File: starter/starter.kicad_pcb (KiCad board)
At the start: 2 copper layers, 70.6 x 59.9 mm, 35 parts, among them J1 Conn_01x04_MountingPin, J2 Conn_01x02, Q1 Q_NMOS_GDS, U1 MCP1416, U2 LM1117DT-ADJ, U3 TLC555xD

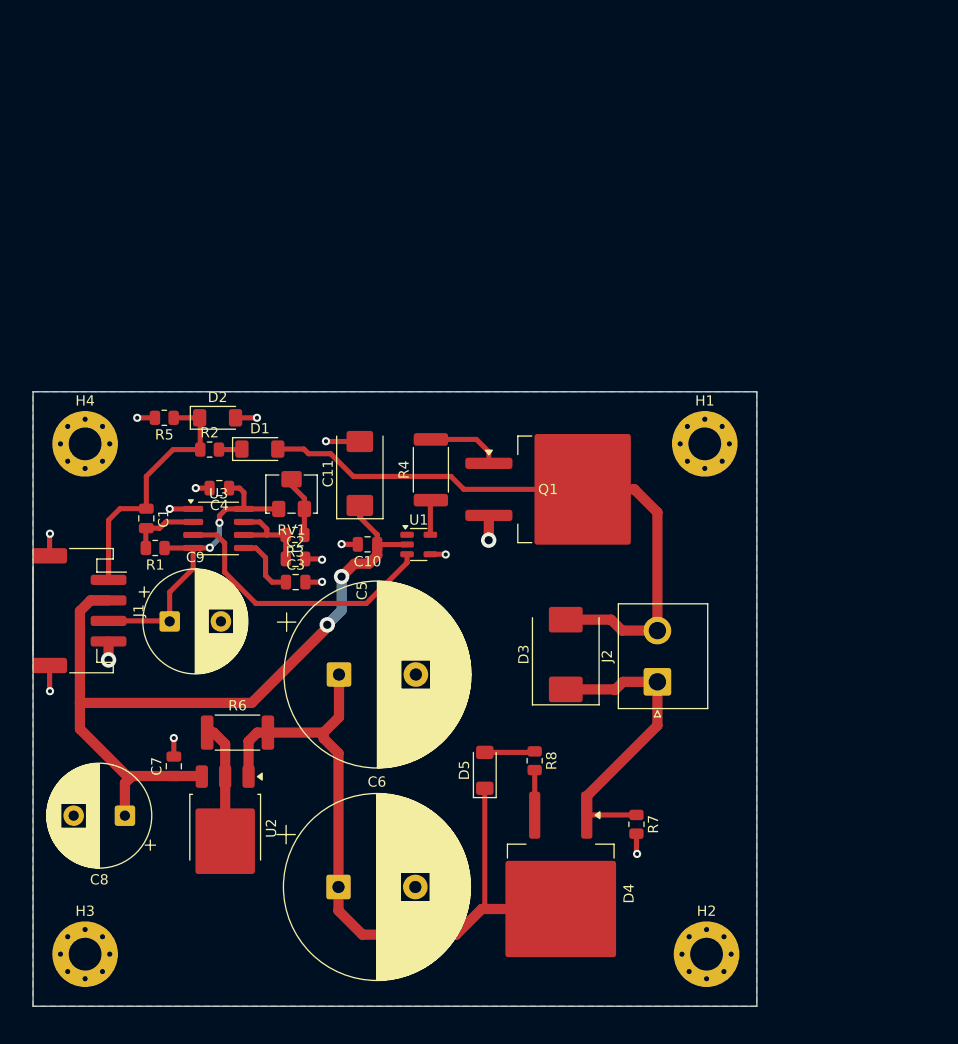
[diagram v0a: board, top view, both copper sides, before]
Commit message: Update starter to rev 2 with I2C IO expander
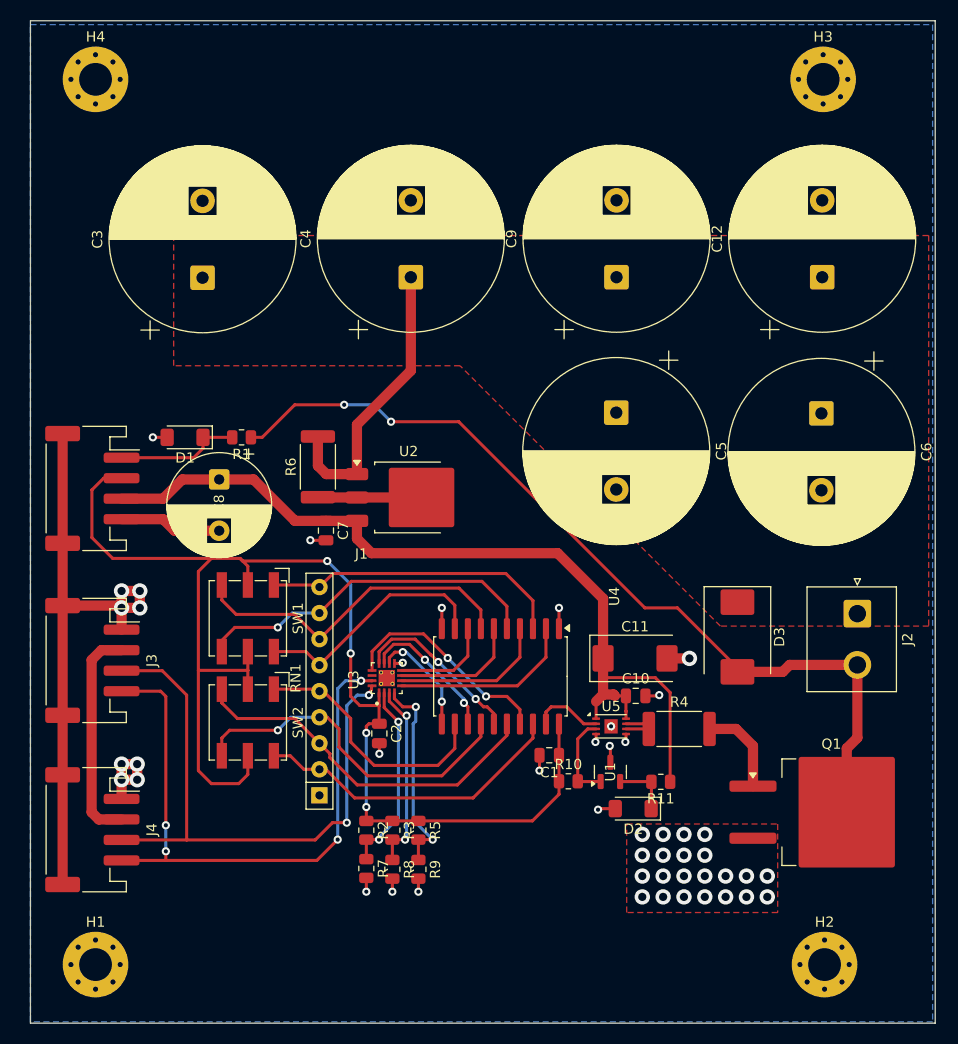
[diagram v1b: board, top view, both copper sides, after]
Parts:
- removed D4: Q_SCR_KAG, Package_TO_SOT_SMD:TO-263-2
- removed D5: D_Zener, Diode_SMD:D_MiniMELF
- removed RV1: R_Potentiometer, Potentiometer_SMD:Potentiometer_Bourns_3214W_Vertical
- added C12: C_Polarized, Capacitor_THT:CP_Radial_D18.0mm_P7.50mm, F.Cu at (106.5, 82.8)
- added J3: Conn_01x04_MountingPin, Connector_JST:JST_PH_S4B-PH-SM4-TB_1x04-1MP_P2.00mm_Horizontal, F.Cu at (35.2, 120.2)
- added J4: Conn_01x04_MountingPin, Connector_JST:JST_PH_S4B-PH-SM4-TB_1x04-1MP_P2.00mm_Horizontal, F.Cu at (35.2, 136.7)
- added R10: R, Resistor_SMD:R_0805_2012Metric, F.Cu at (81.7, 132.0)
- added R11: R, Resistor_SMD:R_0805_2012Metric, F.Cu at (90.7, 132.0)
- added R9: R, Resistor_SMD:R_0805_2012Metric, F.Cu at (67.1, 140.6)
- added RN1: R_Network08, Resistor_THT:R_Array_SIP9, F.Cu at (57.4, 133.3)
- added SW1: SW_Coded_SH-7050, Button_Switch_SMD:Nidec_Copal_SH-7010A, F.Cu at (50.4, 116.1)
- added SW2: SW_Coded_SH-7050, Button_Switch_SMD:Nidec_Copal_SH-7010A, F.Cu at (50.4, 126.2)
- added U4: 74HC688, Package_SO:SOIC-20W_7.5x12.8mm_P1.27mm, F.Cu at (75.1, 121.7)
- added U5: MCP14A1201xMNY, Package_DFN_QFN:TDFN-8-1EP_3x2mm_P0.5mm_EP1.3x1.4mm, F.Cu at (85.9, 126.6)
- C3, C4: value C -> C_Polarized; footprint Capacitor_SMD:C_0805_2012Metric -> Capacitor_THT:CP_Radial_D18.0mm_P7.50mm
- C9: footprint Capacitor_THT:CP_Radial_D10.0mm_P5.00mm -> Capacitor_THT:CP_Radial_D18.0mm_P7.50mm
- D1: value D -> D_Zener
- U1: value MCP1416 -> MCP100-475D; footprint Package_TO_SOT_SMD:SOT-23-5 -> Package_TO_SOT_SMD:SOT-23
- U3: value TLC555xD -> PCF8574RGTR; footprint Package_SO:SOIC-8_3.9x4.9mm_P1.27mm -> th:QFN50P300X300X100-17N
- moved H3 111.7 mm to (106.5, 63.5)
- moved H1 78.2 mm to (35.6, 149.9)
- moved C6 66.0 mm to (106.4, 96.1), turned to -90 degrees
- moved D2 55.7 mm to (88.0, 134.6), turned to 180 degrees
- moved C9 55.0 mm to (86.4, 82.8), turned to 90 degrees
- moved R5 47.3 mm to (67.1, 136.8), turned to -90 degrees
- moved C1 45.6 mm to (79.8, 129.4), turned to 180 degrees
- moved Q1 40.7 mm to (107.3, 135.0)
- moved R2 40.2 mm to (62.0, 136.8), turned to -90 degrees
- moved C5 37.2 mm to (86.4, 96.0), turned to -90 degrees
- moved U2 36.9 mm to (66.1, 104.3), turned to 0 degrees
- moved H4 35.6 mm to (35.6, 63.5)
- moved R4 35.0 mm to (92.5, 126.9), turned to 0 degrees
- moved C8 34.1 mm to (47.6, 102.5), turned to -90 degrees
- moved C11 32.3 mm to (88.2, 120.0), turned to 0 degrees
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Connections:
- C1 pad 1: Net-(D2-K) -> +3.3V
- C1 pad 2: Net-(U3-TR) -> GND
- C2 pad 1: Net-(U3-DIS) -> +3.3V
- C3 pad 1: Net-(U3-CV) -> Net-(D3-K)
- C4 pad 1: +3.3V -> Net-(D3-K)
- C5 pad 1: Net-(D4-A) -> Net-(D3-K)
- C6 pad 1: Net-(D4-A) -> Net-(D3-K)
- C9 pad 1: +3.3V -> Net-(D3-K)
- D1 pad 2: Net-(D1-A) -> GND
- D3 pad 2: Net-(D1-A) -> Net-(D3-A)
- J1 pad 1: Net-(D2-K) -> Net-(D1-K)
- J1 pad 2: +12V -> +3.3V
- J1 pad 3: +3.3V -> +12V
- J2 pad 2: Net-(D1-A) -> Net-(D3-A)
- Q1 pad 2: Net-(D1-A) -> Net-(D3-A)
- R1 pad 1: +3.3V -> Net-(D3-A)
- R1 pad 2: Net-(U3-TR) -> Net-(D1-K)
- R2 pad 1: Net-(D2-K) -> +3.3V
- R2 pad 2: Net-(D1-K) -> Net-(U3-A0)
- R3 pad 1: Net-(R3-Pad1) -> +3.3V
- R3 pad 2: Net-(U3-DIS) -> Net-(U3-A1)
- R4 pad 1: Net-(U1-OUT) -> Net-(R4-Pad1)
- R5 pad 1: Net-(D2-K) -> +3.3V
- R5 pad 2: GND -> Net-(U3-A2)
- R6 pad 2: Net-(D4-A) -> Net-(D3-K)
- R7 pad 1: Net-(D3-K) -> Net-(U3-A0)
- R8 pad 1: Net-(D5-A) -> Net-(U3-A1)
- R8 pad 2: Net-(D4-G) -> GND
- U1 pad 1: unconnected-(U1-NC-Pad1) -> Net-(U1-~{RST})
- U1 pad 2: +12V -> Net-(D2-K)
- U1 pad 3: Net-(U1-IN) -> GND
- U2 pad 1: Net-(D4-A) -> Net-(D3-K)
- U3 pad 1: GND -> +3.3V
- U3 pad 2: Net-(U3-TR) -> Net-(U3-A0)
- U3 pad 3: Net-(U1-IN) -> Net-(U3-A1)
- U3 pad 4: +3.3V -> Net-(U3-A2)
- U3 pad 5: Net-(U3-CV) -> Net-(U3-P0)
- U3 pad 6: Net-(U3-DIS) -> Net-(U3-P1)
- U3 pad 7: Net-(U3-DIS) -> Net-(U3-P2)
- U3 pad 8: +3.3V -> Net-(U3-P3)
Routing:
- net +3.3V: track 31.3 -> 129.7 mm, vias 2 -> 4
- net Net-(D3-A): track 0.00 -> 86.6 mm, vias 0 -> 2
- net Net-(D4-A): track 71.0 -> 0.00 mm
- net GND: track 29.9 -> 99.5 mm, vias 15 -> 47
- net SCL: track 0.00 -> 60.9 mm, vias 0 -> 4
- net Net-(D1-A): track 60.5 -> 0.00 mm
- net SDA: track 0.00 -> 59.2 mm, vias 0 -> 2
- net Net-(RN1-R2): track 0.00 -> 35.8 mm
- net Net-(RN1-R7): track 0.00 -> 34.5 mm, vias 0 -> 1
- net Net-(RN1-R3): track 0.00 -> 34.1 mm, vias 0 -> 1
- net Net-(RN1-R6): track 0.00 -> 33.1 mm
- net Net-(RN1-R1): track 0.00 -> 30.8 mm
- net Net-(RN1-R8): track 0.00 -> 29.7 mm
- net Net-(U1-IN): track 27.8 -> 0.00 mm
- net Net-(RN1-R4): track 0.00 -> 25.1 mm
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- added copper zone on F.Cu, net GND
- added copper zone on F.Cu, net Net-(D3-K)
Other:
- board size 70.6 x 59.9 mm -> 88.3 x 97.8 mm

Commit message: Add high power connector
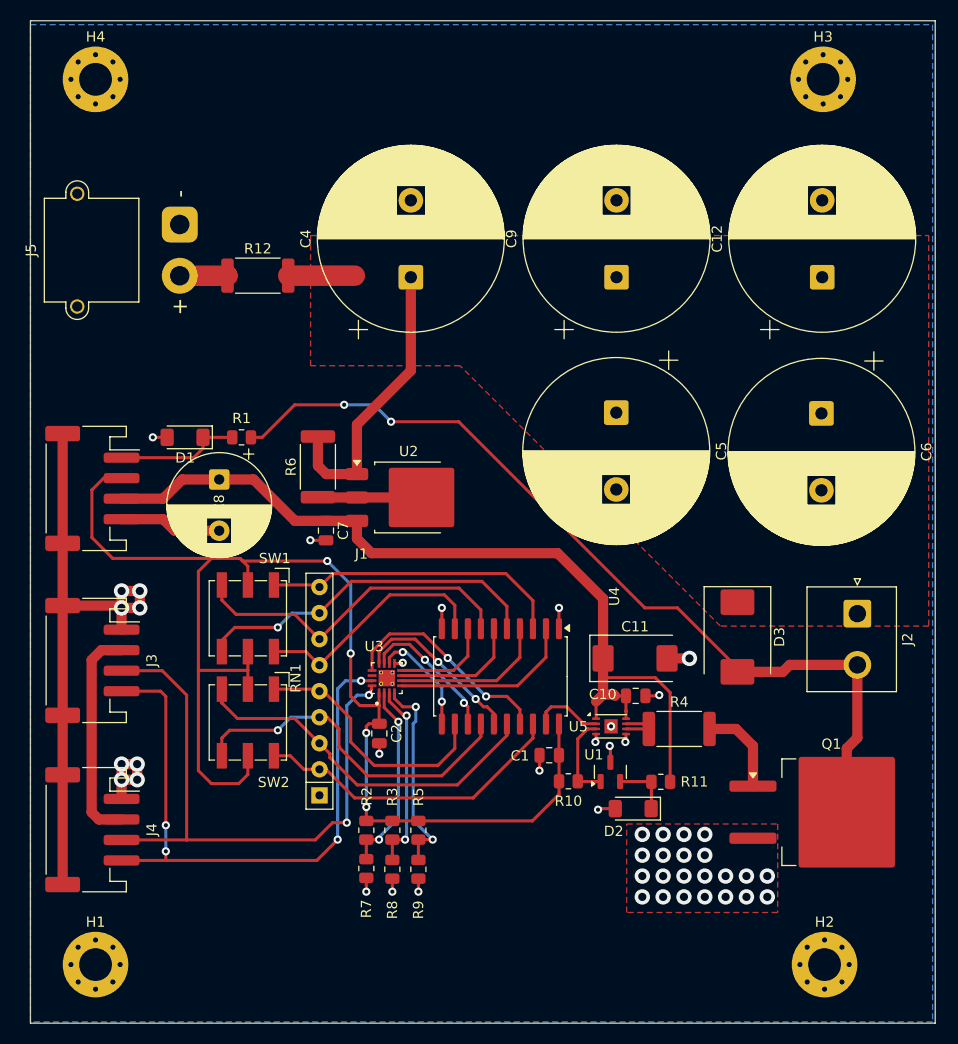
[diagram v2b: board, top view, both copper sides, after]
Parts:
- removed C3: C_Polarized, Capacitor_THT:CP_Radial_D18.0mm_P7.50mm
- added J5: Conn_01x02_MountingPin, Connector_AMASS:AMASS_XT30PW-M_1x02_P2.50mm_Horizontal, F.Cu at (43.8, 77.7)
- added R12: R, Resistor_SMD:R_2512_6332Metric, F.Cu at (51.4, 82.7)
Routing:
- net Net-(D3-K): track 28.4 -> 34.9 mm
- net Net-(J5-Pin_2): track 0.00 -> 4.66 mm
